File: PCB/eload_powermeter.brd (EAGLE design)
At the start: 100 x 100 mm, 66 parts, among them IC1 ADS1115_IC, IC2 AD826R, IC3 TP4056, IC4 FS312F-G, IC5 MT3608, K1 HJR-4102E, K2 TXD2SA-4.5V, Q1 BSS123, Q2 YSX321SL20H, Q3 BSS123, Q4 IRF520, Q5 BSS123, SW1 ENCODER, U1 ATMEGA328P-AU

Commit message: finish boost circuit, start reverse surface mount led
Finishing the boost converter circuit and selecting the inductor and the schottky diode.
Starting with the footprint of the reverse surface mount led.
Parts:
- removed L1: DR74, inductors:DR74
- added C10, C11: 10u, rcl:C0603
- added D3: BAT54, diode:SOT23
- added LED1: (no value), led:CHIPLED_1206
- added LED2: (no value), led:CHIPLED_0805
- added R22: 7k5, rcl:R0603
- added R23: 1k, rcl:R0603
- added SW_PWR1, SW_PWR2: SOLDER_PAD, eload_powermeter:SOLDER_PAD
- added U$2: 22uH, eload_powermeter:R1210
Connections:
- new net N$19: D3.1, IC5.1, R22.2, U$2.2
- new net N$25: IC5.3, R22.1, R23.2
- new net N$26: IC3.5, R10.2, SW_PWR1.P$1, VBAT+.P$1
- net +5V: now also C11.2, D3.3
- net GND: now also C10.1, C11.1, R23.1
- net N$23: now also C10.2, IC5.4, SW_PWR2.P$1, U$2.1; no longer IC3.5, R10.2, VBAT+.P$1
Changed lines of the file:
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@@
 </element>
 <element name="IC5" library="eload_powermeter" package="SOT23-6" value="MT3608" x="-102.87" y="-134.62"/>
-<element name="L1" library="inductors" library_urn="urn:adsk.eagle:library:243" package="DR74" package3d_urn="urn:adsk.eagle:package:15122/1" value="DR74" x="25.4" y="92.71">
-<attribute name="SPICEPREFIX" value="L" x="25.4" y="92.71" size="1.778" layer="27" display="off"/>
+<element name="U$2" library="eload_powermeter" package="R1210" value="22uH" x="-101.6" y="-142.24"/>
+<element name="C10" library="rcl" library_urn="urn:adsk.eagle:library:334" package="C0603" package3d_urn="urn:adsk.eagle:package:23616/2" value="10u" x="-102.87" y="-147.32">
+<attribute name="SPICEPREFIX" value="C" x="-102.87" y="-147.32" size="1.778" layer="27" display="off"/>
 </element>
+<element name="D3" library="diode" library_urn="urn:adsk.eagle:library:210" package="SOT23" package3d_urn="urn:adsk.eagle:package:43389/2" value="BAT54" x="-101.6" y="-161.29"/>
+<element name="C11" library="rcl" library_urn="urn:adsk.eagle:library:334" package="C0603" package3d_urn="urn:adsk.eagle:package:23616/2" value="10u" x="-102.87" y="-167.64">
+<attribute name="SPICEPREFIX" value="C" x="-102.87" y="-167.64" size="1.778" layer="27" display="off"/>
+</element>
+<element name="R22" library="rcl" library_urn="urn:adsk.eagle:library:334" package="R0603" package3d_urn="urn:adsk.eagle:package:23555/2" value="7k5" x="-102.87" y="-172.72">
+<attribute name="SPICEPREFIX" value="R" x="-102.87" y="-172.72" size="1.778" layer="27" display="off"/>
+</element>
+<element name="R23" library="rcl" library_urn="urn:adsk.eagle:library:334" package="R0603" package3d_urn="urn:adsk.eagle:package:23555/2" value="1k" x="-102.87" y="-177.8">
+<attribute name="SPICEPREFIX" value="R" x="-102.87" y="-177.8" size="1.778" layer="27" display="off"/>
+</element>
+<element name="SW_PWR1" library="eload_powermeter" package="SOLDER_PAD" value="SOLDER_PAD" x="-104.14" y="-181.61"/>
+<element name="SW_PWR2" library="eload_powermeter" package="SOLDER_PAD" value="SOLDER_PAD" x="-104.14" y="-185.42"/>
+<element name="LED1" library="led" library_urn="urn:adsk.eagle:library:259" package="CHIPLED_1206" package3d_urn="urn:adsk.eagle:package:15823/2" value="" x="78.74" y="57.15"/>
+<element name="LED2" library="led" library_urn="urn:adsk.eagle:library:259" package="CHIPLED_0805" package3d_urn="urn:adsk.eagle:package:15821/2" value="" x="72.39" y="57.15"/>
 </elements>
 <signals>
@@
 <contactref element="U$1" pad="3"/>
 <contactref element="IC5" pad="2"/>
+<contactref element="C10" pad="1"/>
+<contactref element="R23" pad="1"/>
+<contactref element="C11" pad="1"/>
+<wire x1="-102.87" y1="-135.77" x2="-103.72" y2="-147.32" width="0" layer="19" extent="1-1"/>
 <wire x1="-103.72" y1="-128.27" x2="-102.87" y2="-135.77" width="0" layer="19" extent="1-1"/>
 <wire x1="-103.72" y1="-123.19" x2="-103.72" y2="-128.27" width="0" layer="19" extent="1-1"/>
@@
 <wire x1="-104.14" y1="-73.66" x2="-100.965" y2="-82.61" width="0" layer="19" extent="1-1"/>
 <wire x1="-99.212" y1="-72.39" x2="-104.14" y2="-73.66" width="0" layer="19" extent="1-1"/>
+<wire x1="-103.72" y1="-167.64" x2="-103.72" y2="-147.32" width="0" layer="19" extent="1-1"/>
+<wire x1="-103.72" y1="-177.8" x2="-103.72" y2="-167.64" width="0" layer="19" extent="1-1"/>
 <wire x1="-98.64" y1="-45.72" x2="-99.212" y2="-72.39" width="0" layer="19" extent="1-1"/>
 <wire x1="-98.64" y1="-40.64" x2="-98.64" y2="-45.72" width="0" layer="19" extent="1-1"/>
@@
 <contactref element="U1" pad="18"/>
 <contactref element="U1" pad="20"/>
+<contactref element="C11" pad="2"/>
+<contactref element="D3" pad="3"/>
 <wire x1="21.28466875" y1="70.2040125" x2="46.99" y2="83.82" width="0" layer="19" extent="16-16"/>
 <wire x1="20.15315625" y1="69.072503125" x2="21.28466875" y2="70.2040125" width="0" layer="19" extent="16-16"/>
@@
 <wire x1="-57.15" y1="63.5" x2="-51.94" y2="100.33" width="0" layer="19" extent="1-1"/>
 <wire x1="-90.17" y1="92.71" x2="-51.94" y2="100.33" width="0" layer="19" extent="1-1"/>
+<wire x1="-101.6" y1="-160.19" x2="-57.15" y2="63.5" width="0" layer="19" extent="1-1"/>
+<wire x1="-102.02" y1="-167.64" x2="-101.6" y2="-160.19" width="0" layer="19" extent="1-1"/>
 </signal>
 <signal name="N$8">
@@
 </signal>
 <signal name="N$23">
+<contactref element="C10" pad="2"/>
+<contactref element="IC5" pad="5"/>
+<contactref element="IC5" pad="4"/>
+<contactref element="U$2" pad="1"/>
+<contactref element="SW_PWR2" pad="P$1"/>
+<wire x1="-103" y1="-142.24" x2="-102.02" y2="-147.32" width="0" layer="19" extent="1-1"/>
+<wire x1="-102.87" y1="-133.47" x2="-103" y2="-142.24" width="0" layer="19" extent="1-1"/>
+<wire x1="-101.92" y1="-133.47" x2="-102.87" y2="-133.47" width="0" layer="19" extent="1-1"/>
+<wire x1="-104.14" y1="-185.42" x2="-102.02" y2="-147.32" width="0" layer="19" extent="1-1"/>
+</signal>
+<signal name="N$19">
+<contactref element="U$2" pad="2"/>
+<contactref element="IC5" pad="1"/>
+<contactref element="R22" pad="2"/>
+<contactref element="D3" pad="1"/>
+<wire x1="-103.82" y1="-135.77" x2="-100.2" y2="-142.24" width="0" layer="19" extent="1-1"/>
+<wire x1="-102.55" y1="-162.39" x2="-100.2" y2="-142.24" width="0" layer="19" extent="1-1"/>
+<wire x1="-102.02" y1="-172.72" x2="-102.55" y2="-162.39" width="0" layer="19" extent="1-1"/>
+</signal>
+<signal name="N$25">
+<contactref element="R23" pad="2"/>
+<contactref element="R22" pad="1"/>
+<contactref element="IC5" pad="3"/>
+<wire x1="-103.72" y1="-172.72" x2="-101.92" y2="-135.77" width="0" layer="19" extent="1-1"/>
+<wire x1="-102.02" y1="-177.8" x2="-103.72" y2="-172.72" width="0" layer="19" extent="1-1"/>
+</signal>
+<signal name="N$26">
+<contactref element="R10" pad="2"/>
 <contactref element="IC3" pad="5"/>
-<contactref element="R10" pad="2"/>
 <contactref element="VBAT+" pad="P$1"/>
-<contactref element="IC5" pad="5"/>
-<wire x1="-104.14" y1="-114.3" x2="-102.87" y2="-133.47" width="0" layer="19" extent="1-1"/>
+<contactref element="SW_PWR1" pad="P$1"/>
 <wire x1="-102.02" y1="-107.95" x2="-104.14" y2="-114.3" width="0" layer="19" extent="1-1"/>
 <wire x1="-97.155" y1="-77.41" x2="-102.02" y2="-107.95" width="0" layer="19" extent="1-1"/>
+<wire x1="-104.14" y1="-181.61" x2="-104.14" y2="-114.3" width="0" layer="19" extent="1-1"/>
 </signal>
 </signals>

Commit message: Current Sense Schematic, Switching a few components
Working on the current sense schematic. Cleaning up some other parts. Switching a few components/footprints - primariliy the footprint of the oled screen.
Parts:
- removed C3: 470n, rcl:C1206K
- removed JP1: (no value), PowerMeter:1X04_OLED
- removed JP2, JP3: (no value), pinhead:1X02
- removed K1: HJR-4102E, PowerMeter:FRS1B
- removed LED1: (no value), led:CHIPLED_1206
- removed LED2: (no value), led:CHIPLED_0805
- removed R13: 10k, rcl:M1206
- removed ROPT2, ROPT3: (no value), PowerMeter:0207/10
- removed U$2: 22uH, eload_powermeter:R1210
- added C12: 10u, rcl:C0603
- added D2, D4: BAT54, diode:SOT23
- added L1: 22uH, eload_powermeter:R1210
- added LED_G, LED_R: (no value), eload_powermeter:1206_LED_REVERSE_MOUNT
- added OLED: (no value), eload_powermeter:1X04_OLED
- added Q6, Q7: IRF520, transistor-power:TO220BV
- added R24, R25: 1k, rcl:R0603
- added R26: 7k5, rcl:R0603
- C1, C2: value 470n -> 100n; device rcl:C1206K -> rcl:C0603
- D1: value 1N4148DO35-7 -> 1N4148; device diode:DO35-7 -> diode:SOD123
- R1, R12: value 10k -> 1k; device rcl:M1206 -> rcl:R0603
- R14, R15, R18, R19, R20, R21: device rcl:M1206 -> rcl:R0603
- R16, R2: value 100k -> 90k; device rcl:M1206 -> rcl:R0603
- R17, R3: value 4k7 -> 10k; device rcl:M1206 -> rcl:R0603
- moved C2 348.0 mm to (-90.2, -240.0)
- moved C1 343.5 mm to (-90.2, -234.9)
- moved R12 314.2 mm to (-90.2, -209.6)
- moved R1 311.1 mm to (-90.2, -204.5)
- moved IC5 289.8 mm to (73.7, 95.2), flipped to the bottom
- moved IC4 259.5 mm to (81.3, 95.2), flipped to the bottom
- moved U$1 258.6 mm to (81.3, 87.6), flipped to the bottom
- moved IC3 254.6 mm to (91.4, 88.9), flipped to the bottom, turned to 270 degrees
- moved R23 17.7 mm to (-86.4, -171.4)
- moved SW_PWR1 17.7 mm to (-87.6, -175.3)
- moved C6 17.7 mm to (-81.3, -34.3)
- moved C7 17.7 mm to (-81.3, -39.4)
- moved C9 17.7 mm to (-86.4, -121.9)
- moved R10 17.7 mm to (-86.4, -101.6)
- moved R11 17.7 mm to (-86.4, -105.4)
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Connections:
- removed net N$13: CON_SW2.1, JP3.2, R2.2
- new net N$27: IC3.7, R24.1
- new net N$28: IC3.6, R25.1
- new net N$29: LED_G.C, R24.2
- new net N$30: LED_R.C, R25.2
- new net N$33: IC2.6, R1.1, R12.2
- net +5V: now also K2.1, OLED.VCC; no longer JP1.VCC, K1.1
- net ENC_A: now also C2.2; no longer C3.1
- net ENC_B: now also C1.2; no longer C1.1
- net GND: now also C1.1, C12.1, C2.1, D2.1, D4.1, KK2.A2,5, KK2.B2,5, KK3.A2,5, KK3.B2,5, OLED.GND, R12.1; no longer C1.2, C2.2, C3.2, JP1.GND, JP2.2, R13.1, ROPT2.1
- net N$1: no longer JP2.1, JP3.1
- net N$10: now also K2.12; no longer K1.2
- net N$14: now also CON_SW2.1, K2.4, R2.2; no longer Q4.D
- net N$19: now also L1.2; no longer U$2.2
- net N$2: now also Q6.G, Q7.G
- net N$23: now also L1.1; no longer U$2.1
- net N$3: no longer ROPT2.2, ROPT3.1
- net N$5: now also K2.5
- net N$7: now also IC2.2, R1.2; no longer IC2.6, R12.2
- net N$8: now also C12.2, IC2.3, R26.1; no longer C2.1, IC2.5, R1.2
- net N$9: now also K2.3, Q4.D, Q6.D, Q7.D; no longer IC2.3, R12.1, R13.2
- net PWM: now also R26.2; no longer R1.1
- net SCL: now also IC1.10, OLED.SCL; no longer JP1.SCL
- net SDA: now also OLED.SDA; no longer IC1.10, JP1.SDA
- net SENSE_A0: no longer ROPT3.2
- net SENSE_A1: now also D2.3
- net SENSE_A2: now also D4.3
- net SENSE_A3: now also IC2.5, Q6.S, Q7.S; no longer IC2.2
- net VCC: now also LED_G.A, LED_R.A

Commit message: Finishing Schematic, Starting with Layout
Finishing and cleaning up the schematic, but also replacing some components and optimizing some footprints, for example the ATmega.
Starting with the PCB Layout - placing the components, wiring up the power circuit and the power cuircuit.
Adding an excel file, which shows the data of the chosen values of the current shunt resistors.
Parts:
- removed Q2: YSX321SL20H, eload_powermeter:SMD3225
- removed R19: 90R, rcl:R0603
- removed R21: 10R, rcl:R0603
- removed SV1: (no value), con-lsta:FE06
- removed SW1: ENCODER, eload_powermeter:CI-11
- removed U$1: FS8205, eload_powermeter:SOT23-6
- added C3: 100n, rcl:C0603
- added IC6: FS8205, eload_powermeter:SOT23-6
- added JP1, JP2: (no value), eload_powermeter:2X03
- added R13: 10k, rcl:R0603
- added S3: ALPS_Switch, eload_powermeter:SKHMPXE010
- added S_ENC: ENCODER, eload_powermeter:CI-11
- added Y1: 16MHz, eload_powermeter:RESONATOR-SMD-1:1
- C4, C5: value 12p -> 100n
- IC2: value AD826R -> SGM8582
- KK1, KK2, KK3: device heatsink:SK129 -> eload_powermeter:SK129
- R1: value 1k -> 90k
- R12: value 1k -> 10k
- R18: value 90R -> 18R
- R20: value 10R -> 2R
- U1: value ATMEGA328P-AU -> ATMEGA328P; device eload_powermeter:QFP80P900X900X120-32N -> eload_powermeter:TQFP32-08
- moved C2 348.8 mm to (81.6, 63.5), flipped to the bottom
- moved C1 342.8 mm to (78.4, 63.5), flipped to the bottom, turned to 180 degrees
- moved D4 342.0 mm to (29.8, 66.7), flipped to the bottom
- moved D2 336.4 mm to (34.3, 66.7), flipped to the bottom
- moved SW_PWR2 325.1 mm to (90.8, 92.7), flipped to the bottom
- moved SW_PWR1 319.8 mm to (87.0, 92.7), flipped to the bottom
- moved R12 308.4 mm to (67.9, 55.2), flipped to the bottom, turned to 180 degrees
- moved R23 308.2 mm to (91.4, 80.3), flipped to the bottom
- moved R22 305.9 mm to (91.4, 82.5), flipped to the bottom, turned to 180 degrees
- moved R1 305.7 mm to (67.9, 57.1), flipped to the bottom
- moved R25 301.5 mm to (25.4, 90.8), flipped to the bottom, turned to 270 degrees
- moved C11 301.0 mm to (95.2, 78.7), flipped to the bottom, turned to 180 degrees
- moved Q7 300.1 mm to (78.7, 27.9), turned to 270 degrees
- moved R24 298.8 mm to (22.9, 94.0), flipped to the bottom, turned to 90 degrees
- moved D3 298.1 mm to (95.9, 81.9), flipped to the bottom, turned to 180 degrees
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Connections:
- net N$26 renamed VBAT+
- removed net CS: SV1.1
- removed net VCC: C6.2, C7.2, C8.2, C9.2, IC1.8, IC2.8, IC3.4, IC3.8, IC4.5, LED_G.A, LED_R.A, R10.1, VUSB+.P$1
- new net DTR: C4.2, JP2.1
- new net N$13: IC2.5, K2.9
- new net N$31: C3.2, U1.20
- new net N$40: K2.8, Q1.2, R18.2
- new net RESET: C4.1, JP1.5, R13.1, S3.2, S3.4, U1.29
- new net RX: JP2.5, U1.30
- new net S_1: S1.2
- new net S_ENC: S_ENC.D
- new net TX: JP2.3, U1.31
- new net VBAT-: C8.1, IC4.6, IC6.3, VBAT-.P$1
- new net VUSB: C9.2, IC3.4, IC3.8, LED_G.A, LED_R.A, VUSB+.P$1
- net +5V: now also C5.2, C6.2, C7.2, IC1.8, IC2.8, JP1.2, JP2.2, R13.2; no longer SV1.5, U1.20
- net ENC_A: now also S_ENC.B; no longer SW1.B
- net ENC_B: now also S_ENC.A; no longer SW1.A
- net GND: now also C3.1, IC6.1, JP1.6, JP2.6, S3.1, S3.3, S3.5, S3.6, S_ENC.C, S_ENC.E, Y1.2; no longer C4.1, C8.1, IC4.6, Q2.2, Q2.4, R21.1, SV1.6, SW1.C, SW1.E, U$1.1, U$1.3, VBAT-.P$1
- net MISO: now also JP1.1, U1.16; no longer SV1.4
- net MOSI: now also JP1.4, U1.15; no longer SV1.3
- net N$12: now also Y1.1; no longer C5.2, Q2.1
- net N$15: now also Y1.3; no longer C4.2, Q2.3
- net N$16: now also C8.2, IC4.5, R10.1; no longer SW1.D
- net N$20: now also IC6.4; no longer U$1.4
- net N$22: now also IC6.6; no longer U$1.6
- net N$3: no longer R19.1, R21.2
- net N$7: now also K2.10, Q4.S, Q6.S, Q7.S, R4.2; no longer IC2.2, IC2.7, R1.2
- net SCK: now also JP1.3, U1.17; no longer SV1.2
- net SCL: now also U1.28
- net SDA: now also U1.27
- net SENSE_A0: now also IC2.2, IC2.7, R1.2; no longer Q1.2, R18.2, R19.2
- net SENSE_A3: no longer IC2.5, Q4.S, Q6.S, Q7.S, R4.2
- net S_2: no longer S1.2
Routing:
- net GND: track 14.9 -> 289.3 mm, vias 0 -> 13
- net N$7: track 0.00 -> 148.5 mm, vias 0 -> 2
- net N$1: track 0.00 -> 109.2 mm
- net N$9: track 0.00 -> 98.0 mm
- net N$2: track 0.00 -> 81.8 mm, vias 0 -> 1
- net +5V: track 1.27 -> 69.5 mm
- net VBAT+: track 0.00 -> 35.0 mm
- net N$14: track 0.00 -> 31.1 mm
- net VBAT-: track 0.00 -> 30.4 mm
- net N$13: track 0.00 -> 27.0 mm, vias 0 -> 2
- net N$40: track 0.00 -> 20.5 mm
- net VUSB: track 0.00 -> 20.1 mm
- net SENSE_A0: track 0.00 -> 15.3 mm
- net N$5: track 0.00 -> 14.1 mm
- net N$22: track 0.00 -> 13.0 mm
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
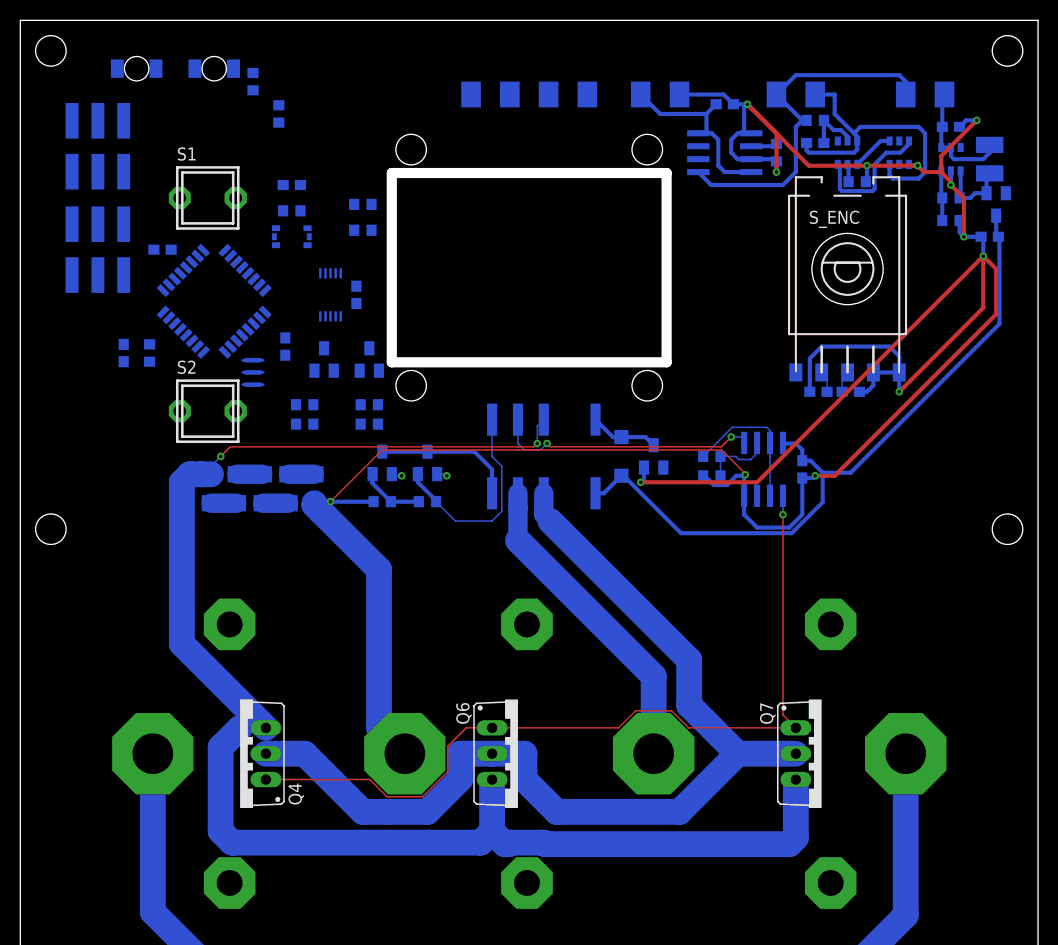
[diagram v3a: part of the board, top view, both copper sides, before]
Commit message: Finish Layout, document schematic with blocks
Routing the last connections of the layout. Starting with the naming on the top panel.
Documenting the schematic by adding functional blocks and descriping them.
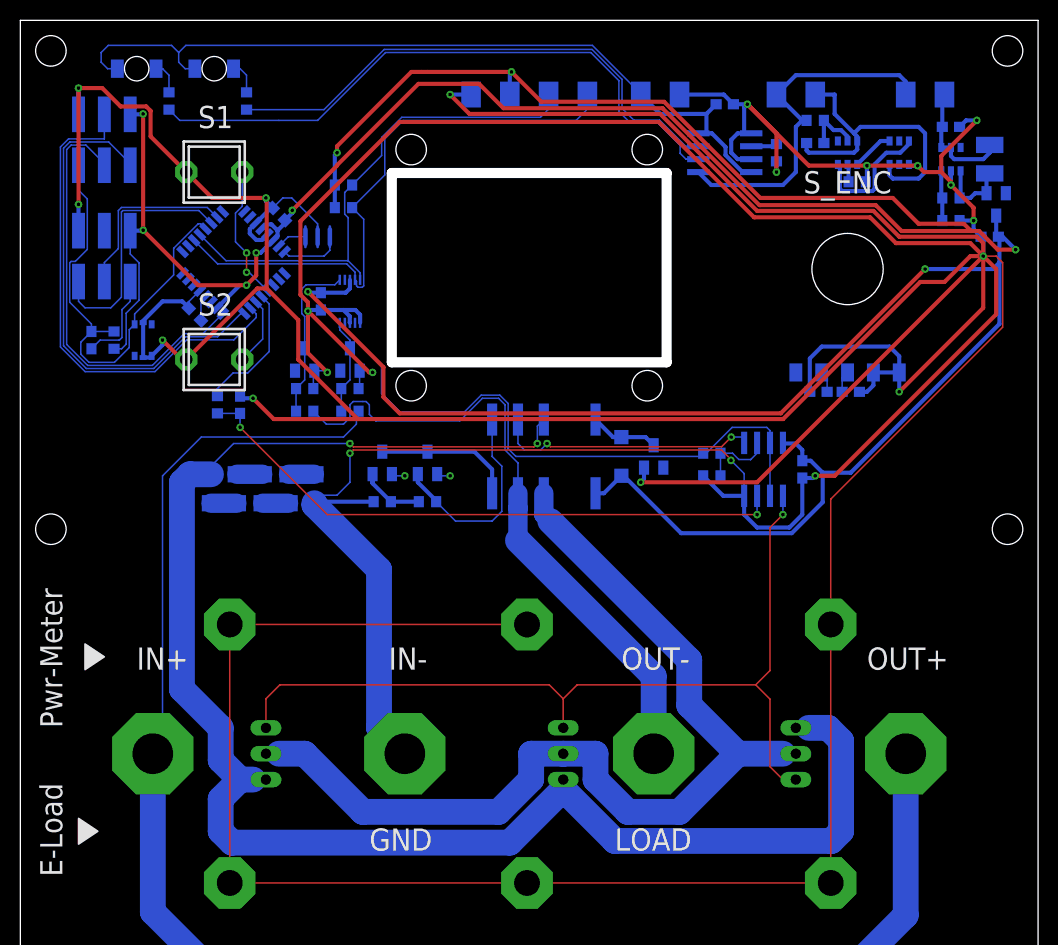
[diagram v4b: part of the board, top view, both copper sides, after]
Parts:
- moved C4 24.9 mm to (6.99, 68.6), turned to 270 degrees
- moved R13 21.6 mm to (9.21, 68.6), turned to 270 degrees
- moved S3 17.8 mm to (12.1, 68.6), turned to 90 degrees
- moved Y1 14.8 mm to (29.2, 78.7), turned to 180 degrees
- moved C5 13.0 mm to (25.4, 81.0), turned to 225 degrees
- moved C12 12.5 mm to (21.6, 62.2)
- moved R25 10.9 mm to (14.6, 92.1), turned to 90 degrees
- moved JP1 10.8 mm to (8.26, 88.3)
- moved JP2 10.8 mm to (8.26, 76.8)
- moved R26 8.38 mm to (19.4, 62.2), turned to 90 degrees
- moved C3 7.10 mm to (17.1, 71.1), turned to 225 degrees
- moved S2 5.12 mm to (19.1, 66.7)
- moved U1 4.26 mm to (21.0, 76.2), turned to 315 degrees
- moved R17 3.98 mm to (32.4, 63.8)
- moved C7 3.55 mm to (29.5, 72.4), turned to 90 degrees
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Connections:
- net GND: no longer S3.3
- net PWM: now also U1.13
- net RESET: no longer S3.2
- net S_1: now also U1.12
- net S_2: now also U1.14
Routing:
- net GND: track 289.3 -> 838.4 mm, vias 13 -> 22
- net +5V: track 69.5 -> 376.0 mm, vias 0 -> 10
- net N$28: track 0.00 -> 61.8 mm
- net N$8: track 0.00 -> 59.8 mm, vias 0 -> 2
- net VUSB: track 20.1 -> 79.3 mm
- net SDA: track 0.00 -> 58.1 mm
- net N$27: track 0.00 -> 52.4 mm
- net SCL: track 0.00 -> 50.7 mm
- net MOSI: track 0.00 -> 50.4 mm
- net N$1: track 109.2 -> 159.4 mm
- net MISO: track 0.00 -> 48.4 mm
- net SENSE_A0: track 15.3 -> 61.4 mm
- net RESET: track 0.00 -> 45.0 mm
- net SCK: track 0.00 -> 42.3 mm
- net N$14: track 31.1 -> 65.4 mm
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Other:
- board text added: "E-Load"
- board text added: "GND"
- board text added: "IN+"
- board text added: "IN-"
- board text added: "LOAD"
- board text added: "OUT+"
- board text added: "OUT-"
- board text added: "Pwr-Meter"
